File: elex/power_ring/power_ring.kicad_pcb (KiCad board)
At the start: 2 copper layers, 118 x 90 mm, 5 parts, among them SW1 R

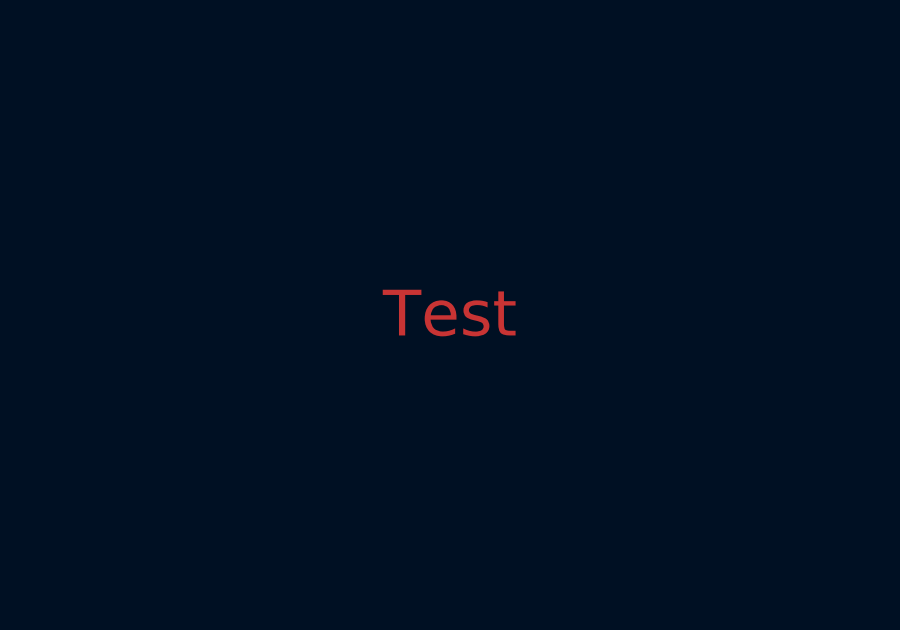
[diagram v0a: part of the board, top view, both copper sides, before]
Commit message: 🔌 : add SugarKube label and document KiBot failure
Add copper "SugarKube" text to power ring PCB and note it in README.
Record outage for KiBot export due to missing pcbnew Python module.
How to test:
- pre-commit run --all-files
- kibot -b elex/power_ring/power_ring.kicad_pro -c .kibot/power_ring.yaml (fails: pcbnew)

Refs: #0
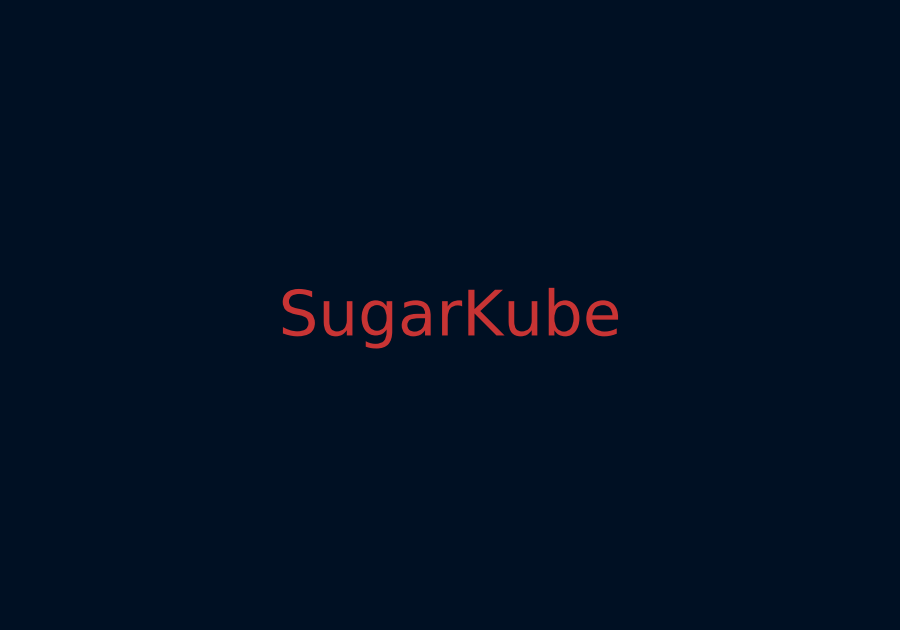
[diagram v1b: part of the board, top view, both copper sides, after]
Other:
- board text added: "SugarKube"
- board text removed: "Test"
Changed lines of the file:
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@@
 		(layer "Edge.Cuts")
 	)
-	(gr_text "Test"
+	(gr_text "SugarKube"
 		(at 159.3 91.4 0)
 		(layer "F.Cu")
